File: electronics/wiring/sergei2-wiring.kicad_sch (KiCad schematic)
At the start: 24 parts

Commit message: Update wiring diagram
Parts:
- M1, M2: renamed from M?; value Motor_DC -> UGRMEM
- M3: renamed from M?; value Motor_DC -> MY1016
- gave numbers to parts that had none: 12
- renumbered DRV_X to DRV_X1, DRV_Y to DRV_Y1, DRV_Z to DRV_Z1, ENC_X to ENC_X1, ENC_Y to ENC_Y1, ENC_Z to ENC_Z1, HOMING_X to HOMING_X1, HOMING_Y to HOMING_Y1, HOMING_Z to HOMING_Z1
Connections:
- net +12V: now also SW3.1, SW4.1
- net ESTOP_INFO: now also J2.13; no longer J2.14
- net IO_GND: now also J2.18, U1. (PWR_ENABLE)
- net MOTOR_FAULT: now also J1.14; no longer J1.16
- net MOTOR_HCURR: now also J1.13; no longer J1.17
- net POWER_GOOD: now also J2.11; no longer J2.12
- net SPINDLE_EN: now also J2.17; no longer J2.15
- net X_A: now also J1.3; no longer J1.4
- net X_B: now also J1.4; no longer J1.5
- net X_HOME: now also J1.16; no longer J1.3
- net Y_A: now also J1.7; no longer J1.9
- net Y_B: now also J1.8; no longer J1.10
- net Y_FWD: now also J1.5; no longer J1.6
- net Y_HOME: now also J1.15; no longer J1.8
- net Y_REV: now also J1.6; no longer J1.7
- net Z_A: now also J1.11; no longer J1.14
- net Z_B: now also J1.12; no longer J1.15
- net Z_FWD: now also J1.9; no longer J1.11
- net Z_HOME: now also J1.17; no longer J1.13
- net Z_REV: now also J1.10; no longer J1.12
- net DOOR_CLOSED_12V: now reaches SW3.2
- net DOOR_CLOSED_12V: now also SW2.C1, SW4.2
- net TOOL_LENGTH_PROBE: now reaches J2.3
- net 3D_PROBE_SENSE: now reaches J2.4
- net 3D_PROBE_CTRL: now reaches J2.5
- net SPINDLE_230V_N: now reaches K1.4, M4.1
- net SPINDLE_230V_L: now reaches K1.5, M4.2
- net +48V_UNFUSED renamed +48V_40A
- removed net FET3_CTRL: J2.17, U1. (POWER_GOOD)
- removed net IOGND: J2.18, U1. (POWER_GOOD)
- removed net MSO2_ACTIVE: J2.13, U1. (POWER_GOOD)
- net MSO2_ACTIVE_12V renamed MSO1_ACTIVE_12V
- net X_Z: no longer names the net of ENC_X1.5 (Z)
- net Y_Z: no longer names the net of ENC_Y1.5 (Z)
- net Z_Z: no longer names the net of ENC_Z1.5 (Z)
- new net FET1_CTRL: J2.15, U1. (PWR_ENABLE)
- new net MSO1_ACTIVE: J2.12, U1. (PWR_ENABLE)
- new net PWR_ENABLE: J2.14, U1. (PWR_ENABLE)
- no-connect marks 3 -> 2
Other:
- note added: "ESTOP BOX"
- note added: "IO WIRING BOX"
- note added: "MODE SWITCH BOX"
- note added: "SW2 and SW3 set ISO16090 operating mode: MSO1: Automatic mode, door closed, spindle active MSO2: Setup mode, door open, spindle stopped MSO3: Manual intervention, door open, spindle active"
- moved on the sheet: DRV_X1, DRV_Y1, DRV_Z1, ENC_X1, ENC_Y1, ENC_Z1, HOMING_X1, HOMING_Y1, HOMING_Z1, M1, M2, M3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

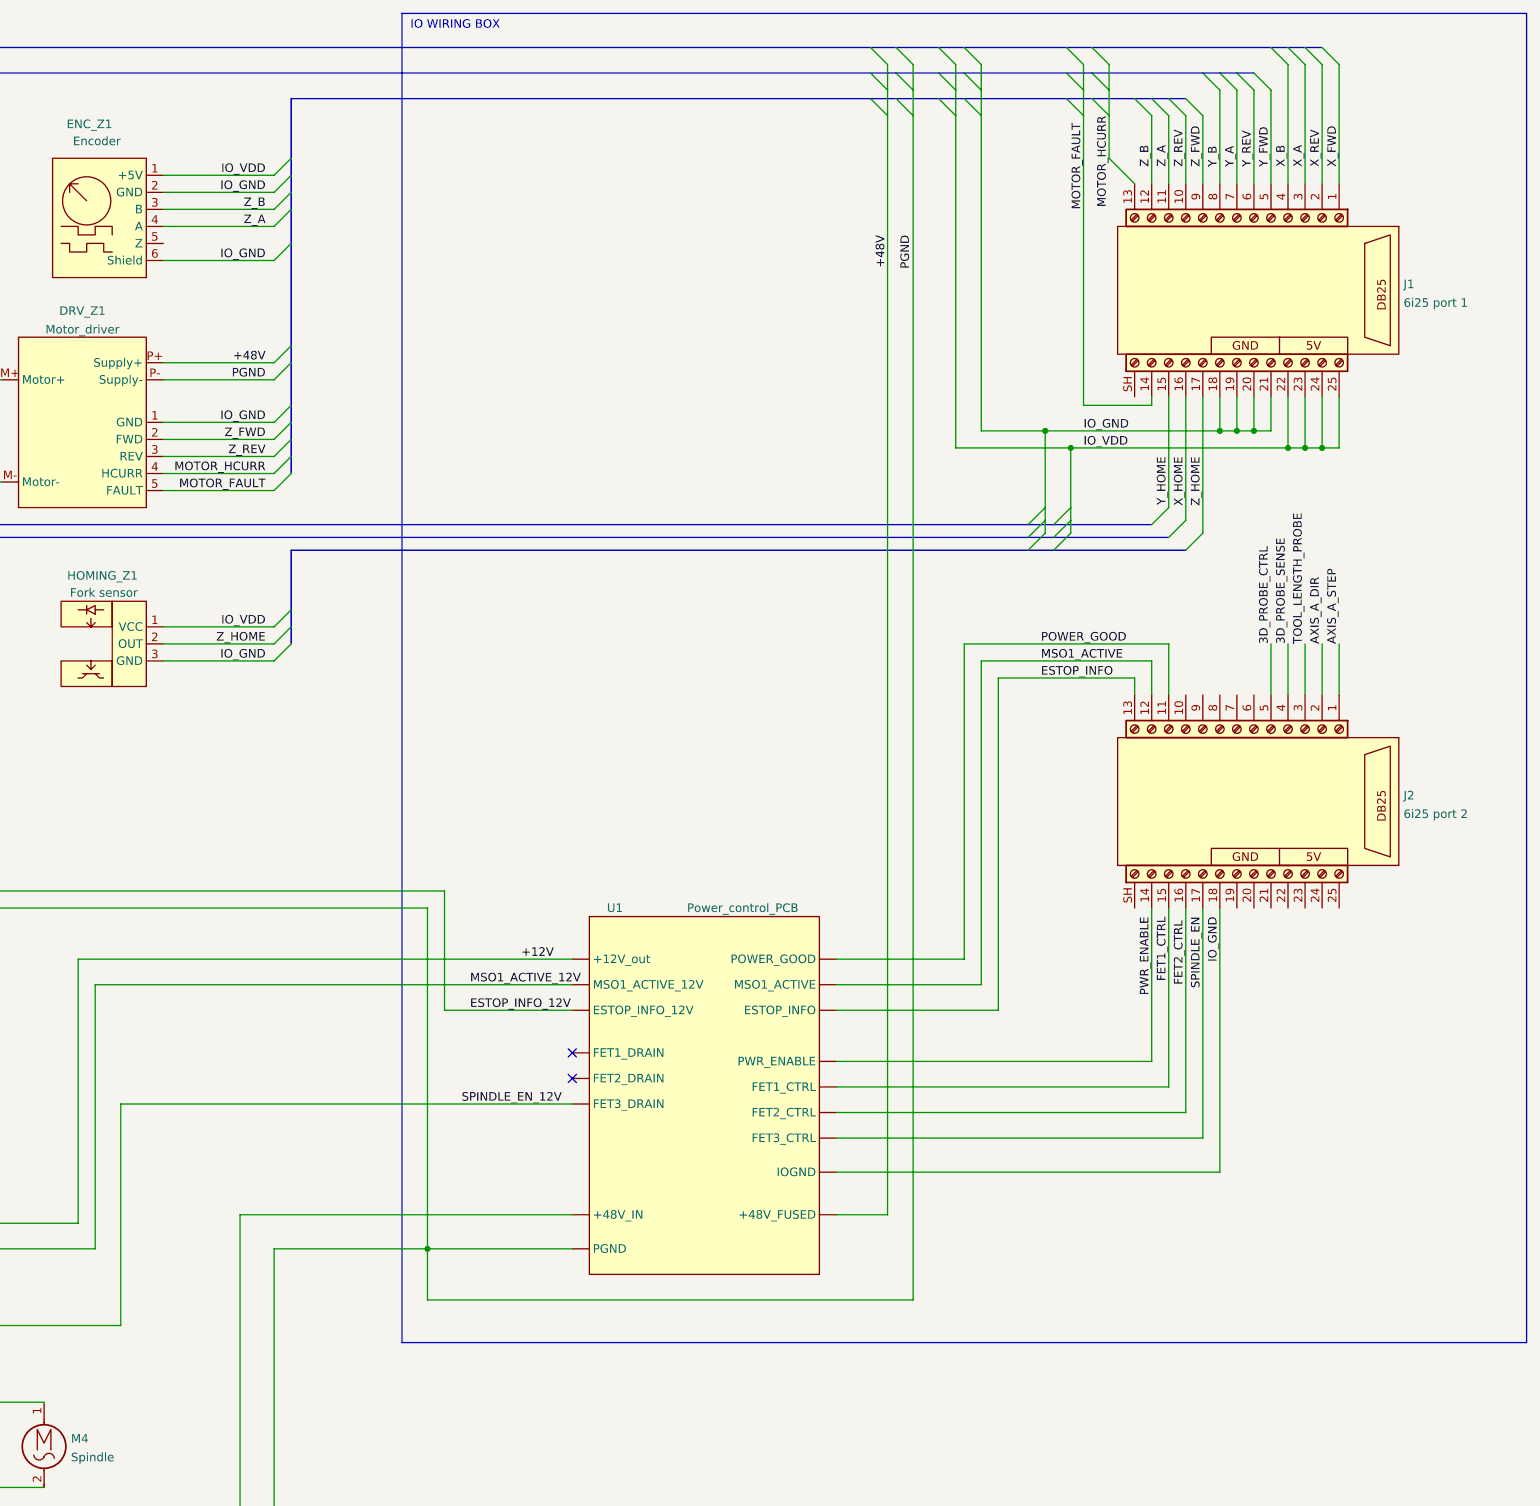
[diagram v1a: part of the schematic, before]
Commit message: Update wiring diagram
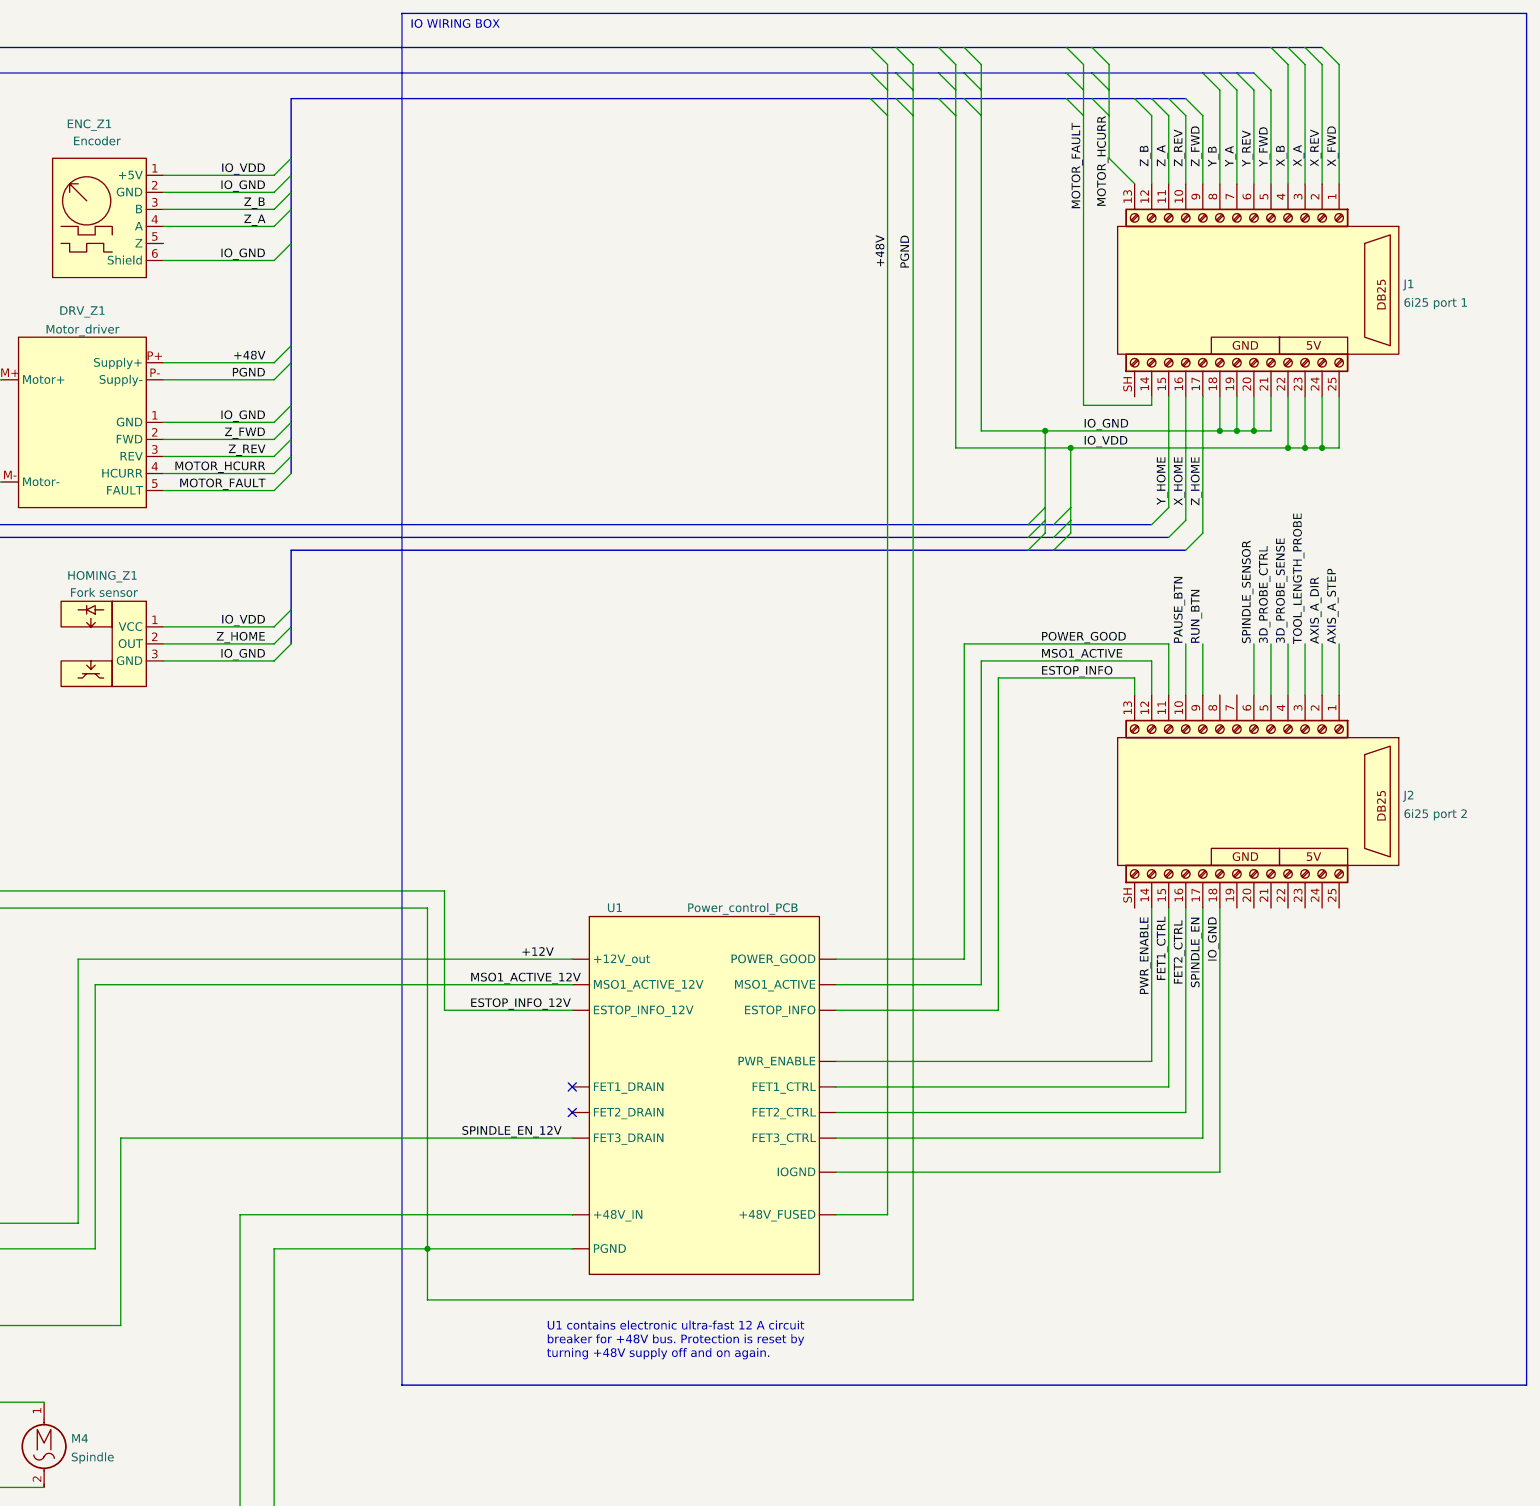
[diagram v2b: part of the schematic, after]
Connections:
- net PAUSE_BTN: now reaches J2.10
- net SPINDLE_SENSOR: now reaches J2.6
- net RUN_BTN: now reaches J2.9
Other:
- note added: "U1 contains electronic ultra-fast 12 A circuit breaker for +48V bus. Protection is reset by turning +48V supply off and on again."
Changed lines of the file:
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@@
   (junction (at 83.82 166.37) (diameter 0) (color 0 0 0 0))
   (junction (at 355.6 80.01) (diameter 0) (color 0 0 0 0))
-  (no_connect (at 254 172.72))
-  (no_connect (at 254 176.53))
+  (no_connect (at 254 177.8))
+  (no_connect (at 254 181.61))
   (bus_entry (at 212.09 78.74) (size -2.54 2.54)
     (stroke (width 0) (type default) (color 0 0 0 0))
@@
     (stroke (width 0.7) (type default) (color 0 0 255 1))
   )
+  (wire (pts (xy 337.82 116.84) (xy 317.5 116.84))
+    (stroke (width 0) (type default) (color 0 0 0 0))
+  )
+  (wire (pts (xy 337.82 119.38) (xy 337.82 116.84))
+    (stroke (width 0) (type default) (color 0 0 0 0))
+  )
   (wire (pts (xy 317.5 116.84) (xy 317.5 166.37))
-    (stroke (width 0) (type default) (color 0 0 0 0))
-  )
-  (wire (pts (xy 337.82 116.84) (xy 317.5 116.84))
-    (stroke (width 0) (type default) (color 0 0 0 0))
-  )
-  (wire (pts (xy 337.82 119.38) (xy 337.82 116.84))
     (stroke (width 0) (type default) (color 0 0 0 0))
   )
@@
     (stroke (width 0) (type default) (color 0 0 0 0))
   )
+  (wire (pts (xy 254 166.37) (xy 234.95 166.37))
+    (stroke (width 0) (type default) (color 0 0 0 0))
+  )
   (wire (pts (xy 234.95 148.59) (xy 234.95 166.37))
-    (stroke (width 0) (type default) (color 0 0 0 0))
-  )
-  (wire (pts (xy 254 166.37) (xy 234.95 166.37))
     (stroke (width 0) (type default) (color 0 0 0 0))
   )
@@
     (stroke (width 0) (type default) (color 0 0 0 0))
   )
+  (wire (pts (xy 342.9 177.8) (xy 342.9 151.13))
+    (stroke (width 0) (type default) (color 0 0 0 0))
+  )
   (wire (pts (xy 293.37 177.8) (xy 342.9 177.8))
-    (stroke (width 0) (type default) (color 0 0 0 0))
-  )
-  (wire (pts (xy 342.9 177.8) (xy 342.9 151.13))
     (stroke (width 0) (type default) (color 0 0 0 0))
   )
@@
     (stroke (width 0) (type default) (color 0 0 0 0))
   )
-  (polyline (pts (xy 228.6 215.9) (xy 396.24 215.9))
-    (stroke (width 0) (type default) (color 0 0 0 0))
-  )
-  (polyline (pts (xy 396.24 17.78) (xy 396.24 215.9))
-    (stroke (width 0) (type default) (color 0 0 0 0))
-  )
-  (polyline (pts (xy 228.6 215.9) (xy 228.6 17.78))
-    (stroke (width 0) (type default) (color 0 0 0 0))
-  )
   (polyline (pts (xy 228.6 17.78) (xy 396.24 17.78))
+    (stroke (width 0) (type default) (color 0 0 0 0))
+  )
+  (polyline (pts (xy 396.24 17.78) (xy 396.24 222.25))
+    (stroke (width 0) (type default) (color 0 0 0 0))
+  )
+  (polyline (pts (xy 228.6 222.25) (xy 396.24 222.25))
+    (stroke (width 0) (type default) (color 0 0 0 0))
+  )
+  (polyline (pts (xy 228.6 222.25) (xy 228.6 17.78))
     (stroke (width 0) (type default) (color 0 0 0 0))
   )
@@
     (stroke (width 0.4) (type default) (color 0 0 0 1))
   )
+  (wire (pts (xy 345.44 111.76) (xy 345.44 119.38))
+    (stroke (width 0) (type default) (color 0 0 0 0))
+  )
   (wire (pts (xy 76.2 83.82) (xy 59.69 83.82))
     (stroke (width 0) (type default) (color 0 0 0 0))
@@
     (stroke (width 0) (type default) (color 0 0 0 0))
   )
+  (wire (pts (xy 345.44 181.61) (xy 345.44 151.13))
+    (stroke (width 0) (type default) (color 0 0 0 0))
+  )
   (wire (pts (xy 293.37 181.61) (xy 345.44 181.61))
-    (stroke (width 0) (type default) (color 0 0 0 0))
-  )
-  (wire (pts (xy 345.44 181.61) (xy 345.44 151.13))
     (stroke (width 0) (type default) (color 0 0 0 0))
   )
@@
     (stroke (width 0) (type default) (color 0 0 0 0))
   )
+  (wire (pts (xy 300.99 196.85) (xy 293.37 196.85))
+    (stroke (width 0) (type default) (color 0 0 0 0))
+  )
   (wire (pts (xy 300.99 33.02) (xy 300.99 196.85))
-    (stroke (width 0) (type default) (color 0 0 0 0))
-  )
-  (wire (pts (xy 300.99 196.85) (xy 293.37 196.85))
     (stroke (width 0) (type default) (color 0 0 0 0))
   )
@@
     (stroke (width 0) (type default) (color 0 0 0 0))
   )
+  (wire (pts (xy 232.41 209.55) (xy 232.41 201.93))
+    (stroke (width 0) (type default) (color 0 0 0 0))
+  )
   (wire (pts (xy 304.8 209.55) (xy 232.41 209.55))
     (stroke (width 0) (type default) (color 0 0 0 0))
   )
-  (wire (pts (xy 232.41 209.55) (xy 232.41 201.93))
-    (stroke (width 0) (type default) (color 0 0 0 0))
-  )
   (wire (pts (xy 76.2 46.99) (xy 59.69 46.99))
     (stroke (width 0) (type default) (color 0 0 0 0))
@@
   )
   (wire (pts (xy 27.94 72.39) (xy 27.94 73.66))
+    (stroke (width 0) (type default) (color 0 0 0 0))
+  )
+  (wire (pts (xy 355.6 111.76) (xy 355.6 119.38))
     (stroke (width 0) (type default) (color 0 0 0 0))
   )
@@
     (stroke (width 0.7) (type default) (color 0 0 255 1))
   )
-  (wire (pts (xy 186.69 180.34) (xy 254 180.34))
-    (stroke (width 0) (type default) (color 0 0 0 0))
-  )
-  (wire (pts (xy 186.69 213.36) (xy 186.69 180.34))
+  (wire (pts (xy 186.69 185.42) (xy 254 185.42))
+    (stroke (width 0) (type default) (color 0 0 0 0))
+  )
+  (wire (pts (xy 186.69 213.36) (xy 186.69 185.42))
     (stroke (width 0) (type default) (color 0 0 0 0))
   )
@@
     (stroke (width 0) (type default) (color 0 0 0 0))
   )
+  (wire (pts (xy 347.98 111.76) (xy 347.98 119.38))
+    (stroke (width 0) (type default) (color 0 0 0 0))
+  )
   (text "SW2 and SW3 set ISO16090 operating mode:\nMSO1: Automatic mode, door closed, spindle active\nMSO2: Setup mode, door open, spindle stopped\nMSO3: Manual intervention, door open, spindle active\n"
     (at 88.9 161.29 0)
@@
     (effects (font (size 1.27 1.27)) (justify left bottom))
   )
+  (text "U1 contains electronic ultra-fast 12 A circuit\nbreaker for +48V bus. Protection is reset by\nturning +48V supply off and on again."
+    (at 250.19 218.44 0)
+    (effects (font (size 1.27 1.27)) (justify left bottom))
+  )
   (text "IO WIRING BOX" (at 229.87 20.32 0)
     (effects (font (size 1.27 1.27)) (justify left bottom))
@@
     (effects (font (size 1.27 1.27)) (justify left bottom))
   )
+  (label "SPINDLE_SENSOR" (at 355.6 111.76 90)
+    (effects (font (size 1.27 1.27)) (justify left bottom))
+  )
   (label "SPINDLE_230V_N" (at 137.16 226.06 0)
     (effects (font (size 1.27 1.27)) (justify left bottom))
@@
     (effects (font (size 1.27 1.27)) (justify right bottom))
   )
+  (label "PAUSE_BTN" (at 345.44 111.76 90)
+    (effects (font (size 1.27 1.27)) (justify left bottom))
+  )
   (label "MOTOR_FAULT" (at 74.93 88.9 180)
     (effects (font (size 1.27 1.27)) (justify right bottom))
   )
+  (label "RUN_BTN" (at 347.98 111.76 90)
+    (effects (font (size 1.27 1.27)) (justify left bottom))
+  )
   (label "IO_GND" (at 74.93 44.45 180)
     (effects (font (size 1.27 1.27)) (justify right bottom))
@@
     (effects (font (size 1.27 1.27)) (justify right bottom))
   )
-  (label "SPINDLE_EN_12V" (at 237.49 180.34 0)
-    (effects (font (size 1.27 1.27)) (justify left bottom))
-  )
+  (label "SPINDLE_EN_12V" (at 237.49 185.42 0)
+    (effects (font (size 1.27 1.27)) (justify left bottom))
+  )

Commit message: Update wiring diagram & motor driver part values
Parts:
- removed K1: ~, symbol Relay:IM12
- removed M4: Spindle, symbol Motor:Motor_AC
- added M?: Spindle, symbol sergei2_wiring:Motor_AC_3PHASE
- added NT?: NetTie_2, symbol Device:NetTie_2
- added PS2: 220V 1.5kW, symbol sergei2_wiring:VFD
- added R?: 1k, symbol Device:R
- added SW?: Run, symbol Switch:SW_Push_LED
- added SW?: Pause, symbol Switch:SW_Push_LED
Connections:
- net FET1_CTRL is gone; now on net PWR_GOOD: J2.15, U1. (STATUS1_IN)
- net SPINDLE_EN_12V is gone; now on net PWR_GOOD: U1. (STATUS1_IN)
- net +12V: now also SW2.C; no longer SW3.1, SW4.1
- net ESTOP_INFO: now also J2.16; no longer J2.13
- net IO_GND: now also PS2. (STATUS), SW?.1, SW?.1
- net MSO1_ACTIVE: now also J2.17; no longer J2.12
- net MSO1_ACTIVE_12V: now also SW3.1, SW4.1; no longer SW2.C
- net PAUSE_BTN: now also J2.11, SW?.2; no longer J2.10
- net RUN_BTN: now also J2.12, SW?.2; no longer J2.9
- net GNDPWR: now reaches J2.SH (SHIELD)
- net GNDPWR: now also J1.SH (SHIELD), NT?.2
- net at PS1.2 (N): now also SW1.NC2B, PS2. (STATUS); no longer SW2.A
- net at PS1.3 (L): now also SW1.NC1B, PS2. (STATUS); no longer SW2.B
- net PWR_GOOD: now reaches U1. (STATUS1_IN)
- net at TP1.1: now also SW2.B1, SW2.B2; no longer SW1.NC1A
- net at SW1.NC2A: now also SW2.A; no longer TP2.1
- net at SW2.A1, SW2.A2: now also TP2.1; no longer SW1.NC2B
- net DOOR_CLOSED_12V renamed MSO1_SELECTED
- net MSO1_SELECTED: now also R?.2, SW?.4 (A)
- removed net FET2_CTRL: J2.16, U1. (PWR_ENABLE)
- net GND renamed PGND
- net PGND: now also NT?.1, SW?.3 (K)
- removed net POWER_GOOD: J2.11, U1. (PWR_ENABLE)
- removed net SPINDLE_EN: J2.17, U1. (PWR_ENABLE)
- net SPINDLE_SENSOR: no longer names the net of J2.6
- new net: SW1.NC1A, SW2.B
- new net: M?.1, PS2. (STATUS)
- new net: M?.2, PS2. (STATUS)
- new net: M?.3, PS2. (STATUS)
- new net PAUSE_RUN_INDICATOR: J2.13, U1. (STATUS1_IN)
- new net PAUSE_RUN_INDICATOR_12V: R?.1, SW?.3 (K), SW?.4 (A), U1. (STATUS1_IN)
- new net SPINDLE_CTRL: J2.10, PS2. (STATUS)
- new net SPINDLE_STATUS: J2.9, PS2. (STATUS)
- no-connect marks 2 -> 6
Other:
- moved on the sheet: DRV_X1, DRV_Y1, DRV_Z1, ENC_X1, ENC_Y1, ENC_Z1, HOMING_X1, HOMING_Y1, HOMING_Z1, J1, J2, M1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

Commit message: Update schematics
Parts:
- removed SW3: Door switch override, symbol Switch:SW_Push
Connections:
- net ESTOP_INFO_12V: now also SW1.NO1A; no longer SW1.NO1B
- net PGND: now also SW1.NO1B; no longer SW1.NO1A
